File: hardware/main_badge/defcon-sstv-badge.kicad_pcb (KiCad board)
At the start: 4 copper layers, 185.7 x 199 mm, 136 parts, among them J1 Conn_01x02, J10 Micro_SD_Card, J11 Mechanical/Grounds, J12 Mechanical/Grounds, J2 USB4105-GF-A, J3 ILI9341 Display Module, J4 Conn_02x09_Odd_Even, J5 SAO1, J6 SAO2, J7 Conn_01x08_Socket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

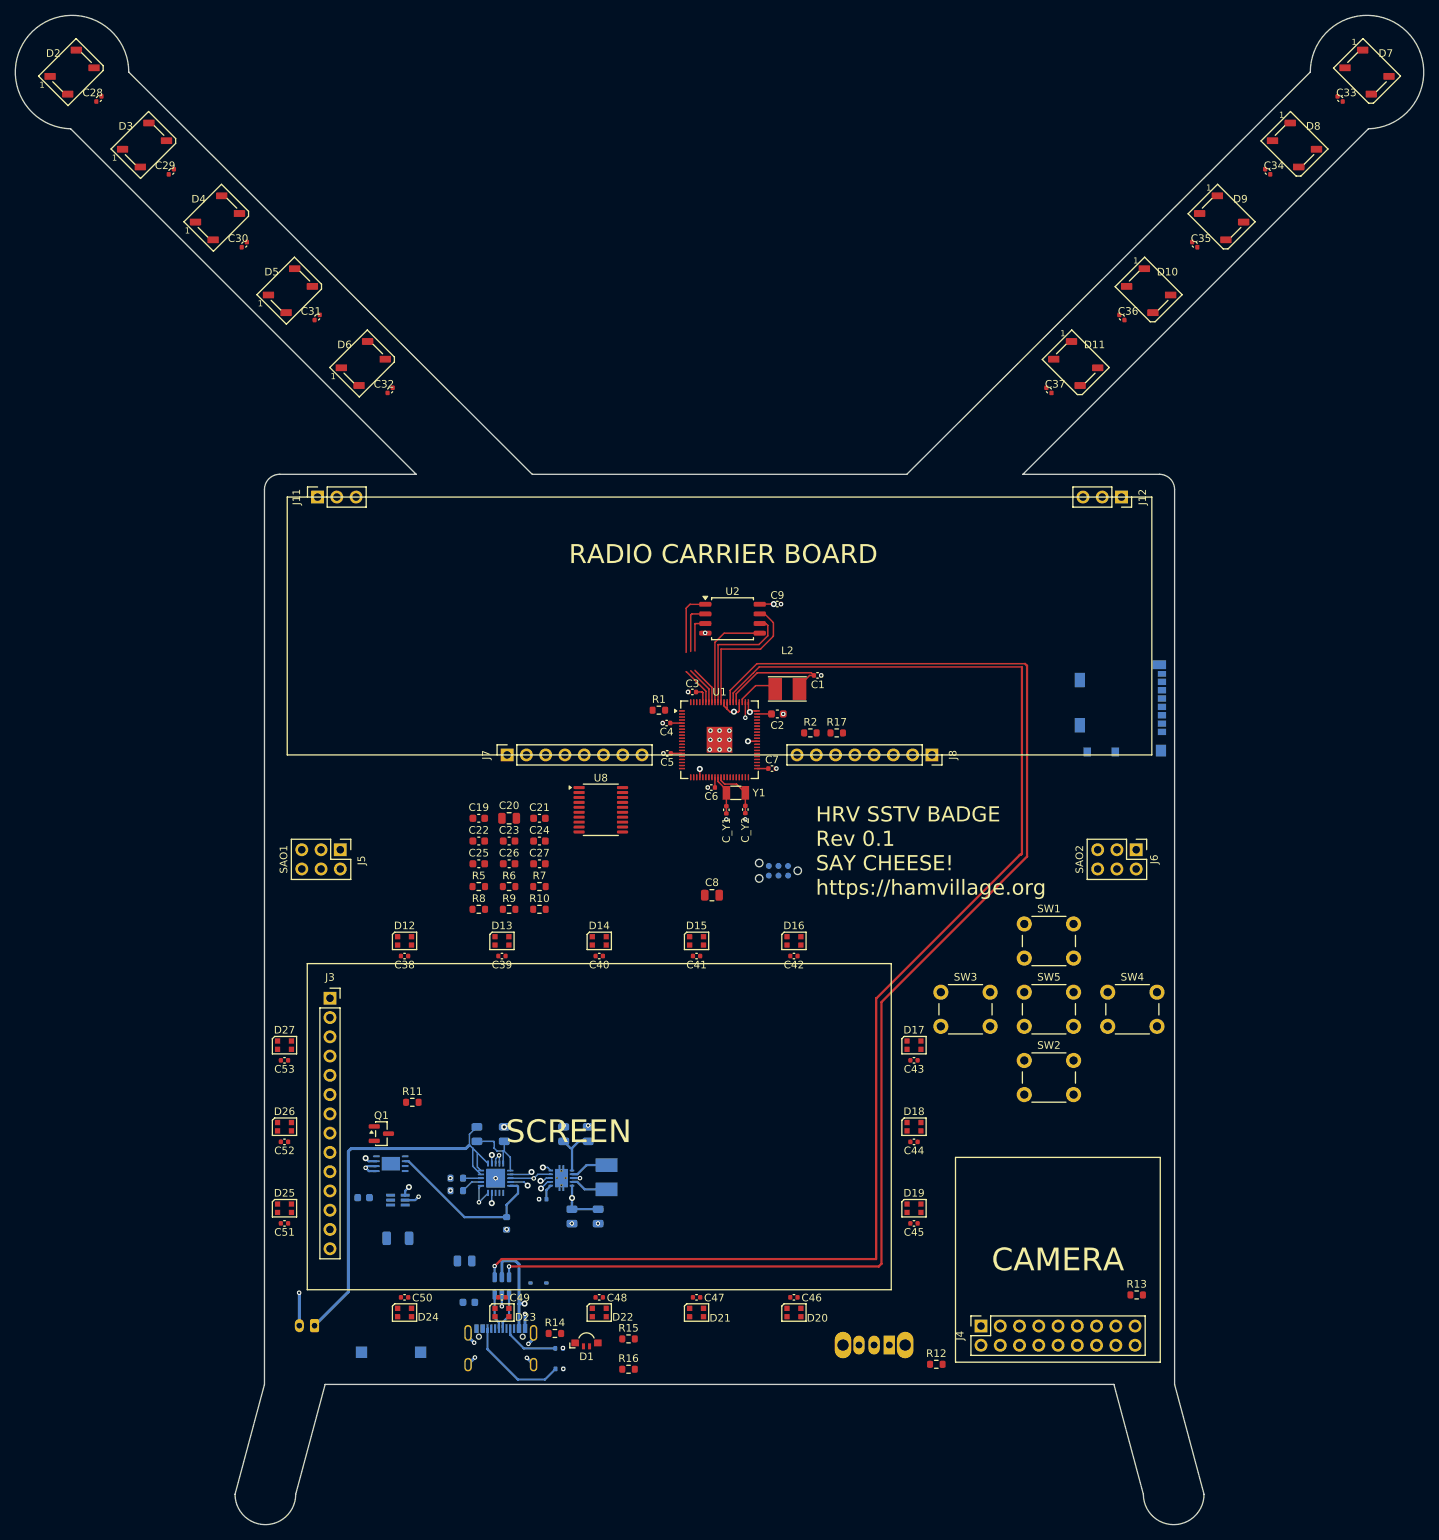
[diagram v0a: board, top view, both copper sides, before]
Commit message: traces all fubar, might delete them all and start over.
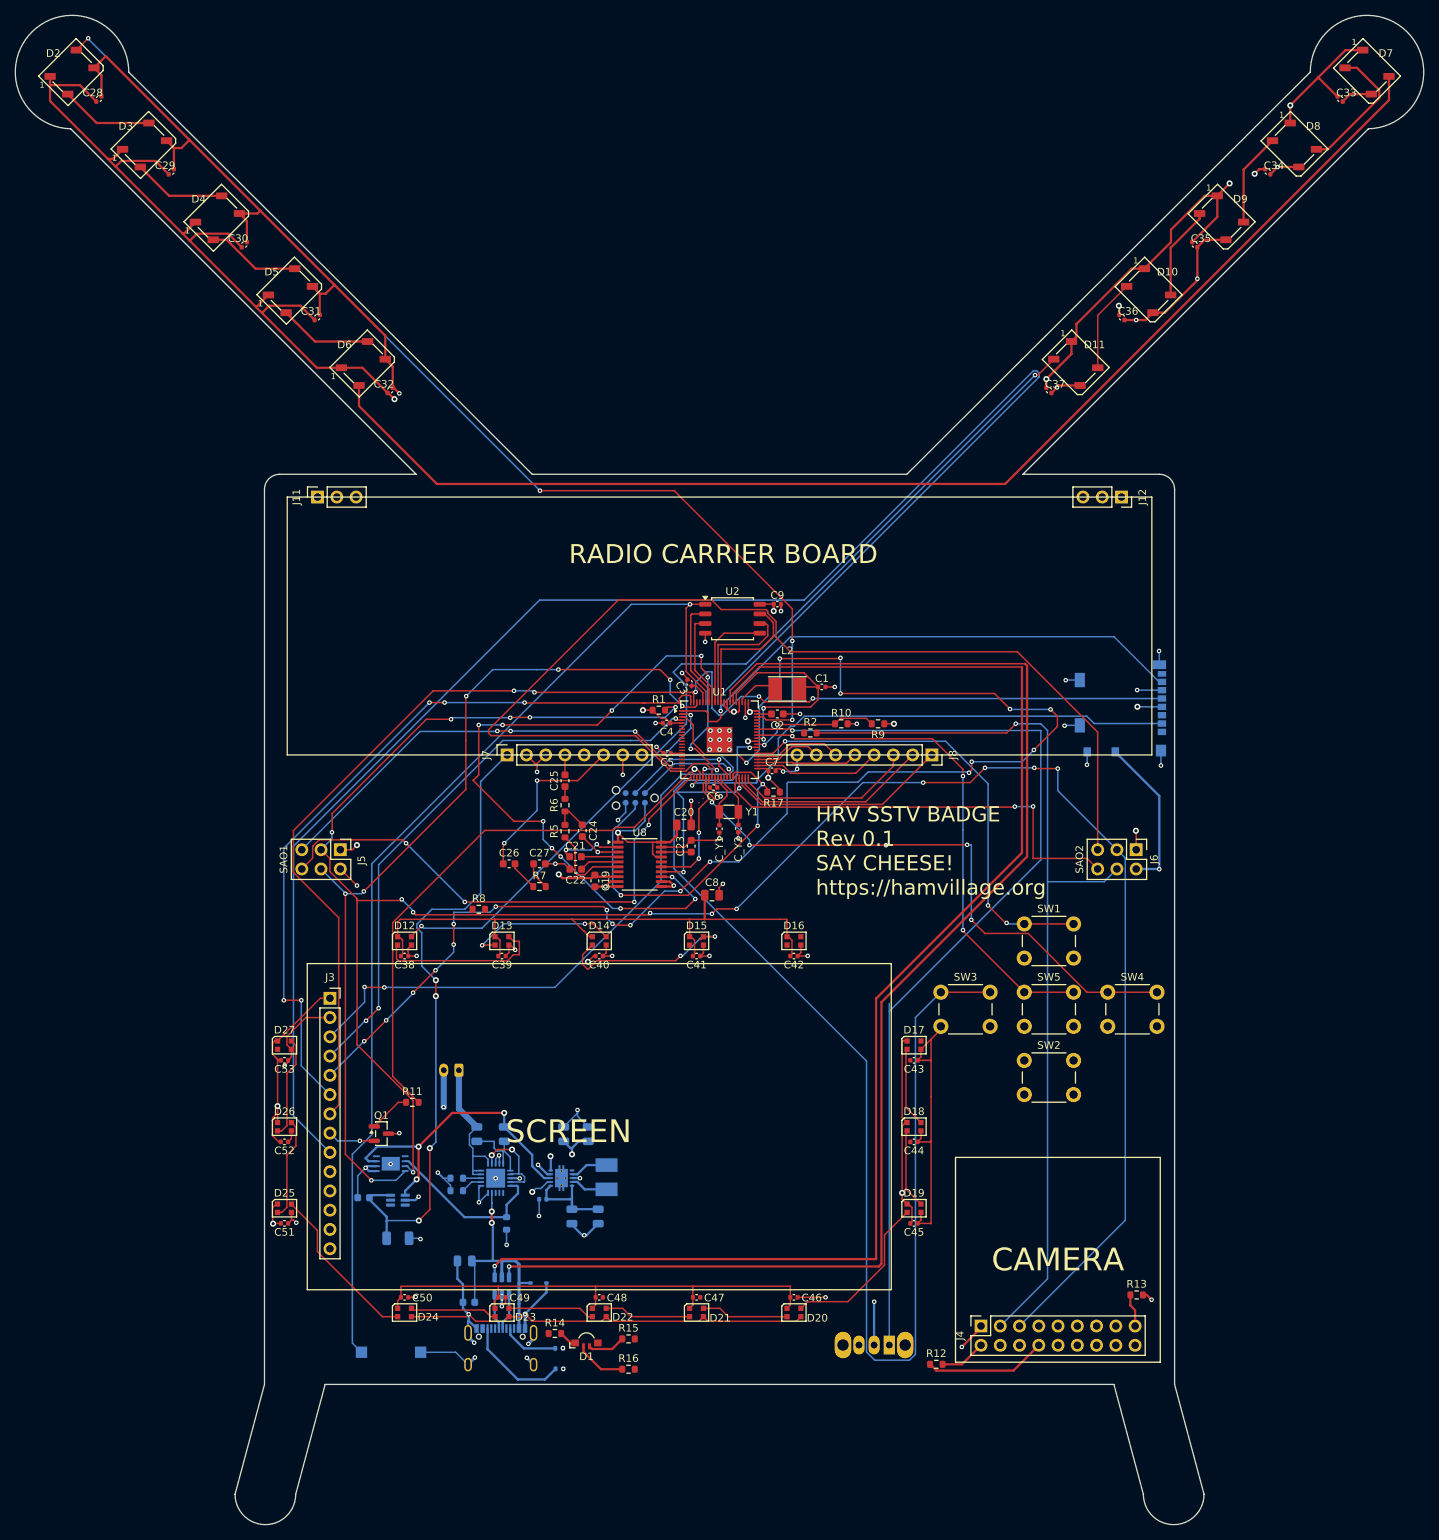
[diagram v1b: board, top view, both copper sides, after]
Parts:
- moved R9 54.4 mm to (80.9, 32.9), turned to 180 degrees
- moved R10 46.7 mm to (76.0, 32.9)
- moved J1 38.7 mm to (25.6, 78.6)
- moved C23 24.0 mm to (56.3, 49.0), turned to 90 degrees
- moved C20 23.1 mm to (55.3, 46.2)
- moved J9 21.2 mm to (48.9, 42.7)
- moved C19 17.4 mm to (43.6, 53.6), turned to -90 degrees
- moved C25 15.8 mm to (39.6, 40.4), turned to 90 degrees
- moved R5 13.5 mm to (39.6, 47.1), turned to 90 degrees
- moved C22 13.3 mm to (41.0, 52.1), turned to 180 degrees
- moved R6 13.0 mm to (39.6, 43.6), turned to 90 degrees
- moved R17 11.4 mm to (67.1, 41.9), turned to 180 degrees
- moved U8 8.83 mm to (49.5, 51.4)
- moved C21 6.94 mm to (41.0, 50.4)
- moved C24 5.82 mm to (41.9, 47.0), turned to -90 degrees
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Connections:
- U1 pad 38: SA818_TX -> SA818_RX
- U1 pad 39: SA818_RX -> SA818_TX
- U1 pad 44: SA818_SQ -> SA818_ID
- U1 pad 45: SA818_ID -> SA818_SQ
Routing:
- net +3V3: track 32.7 -> 462.3 mm, vias 7 -> 26
- net GND: track 46.4 -> 441.4 mm, vias 45 -> 78
- net SPI_MISO: track 0.00 -> 301.2 mm, vias 0 -> 1
- net I2C_SDA: track 0.00 -> 291.4 mm, vias 0 -> 15
- net I2C_SCL: track 0.00 -> 240.4 mm, vias 0 -> 8
- net DISP_DC: track 0.00 -> 195.7 mm, vias 0 -> 21
- net SPI_SCK: track 0.00 -> 172.4 mm, vias 0 -> 5
- net Net-(D6-DOUT): track 0.00 -> 166.9 mm
- net DPAD_LEFT: track 0.00 -> 162.9 mm, vias 0 -> 1
- net LED_DATA: track 0.00 -> 145.8 mm, vias 0 -> 4
- net SAO2_GPIO1: track 0.00 -> 145.2 mm
- net AIRPLANE: track 0.00 -> 127.8 mm, vias 0 -> 1
- net Net-(U1-~{QSPI_SS}): track 13.7 -> 138.3 mm, vias 0 -> 1
- net Net-(D11-DOUT): track 0.00 -> 122.9 mm, vias 0 -> 2
- net I2S_BCK: track 0.00 -> 105.7 mm, vias 0 -> 14
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- added copper zone on In1.Cu, net GND

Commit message: clean PCB, prior to rewiring for clean board design
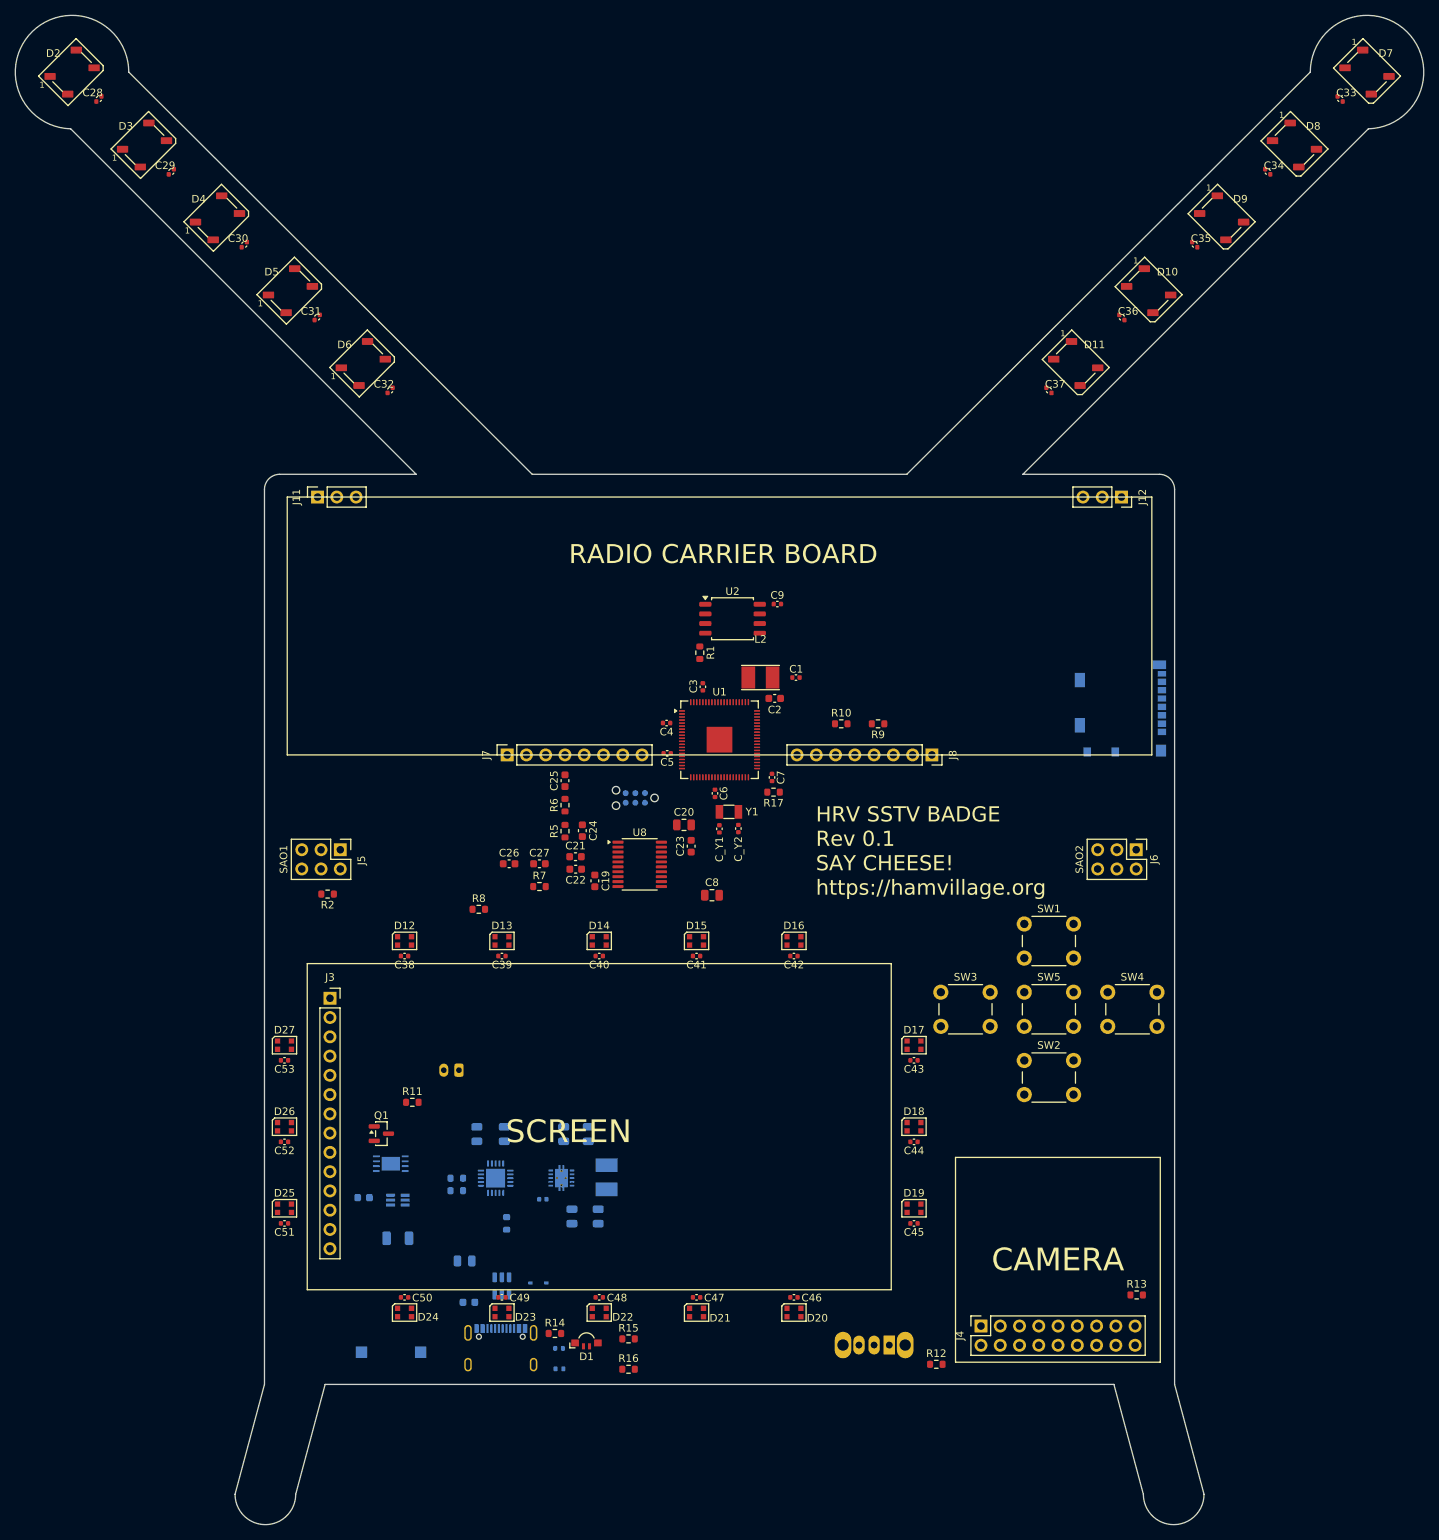
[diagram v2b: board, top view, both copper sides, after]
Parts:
- moved R2 67.1 mm to (8.32, 55.4), turned to 180 degrees
- moved R1 9.30 mm to (57.4, 23.5), turned to -90 degrees
- moved L2 3.84 mm to (65.4, 26.8)
- moved C1 3.61 mm to (70.1, 26.8)
- moved C2 2.08 mm to (67.3, 29.6)
- moved C3 1.83 mm to (57.8, 28.0), turned to 90 degrees
- moved C7 0.87 mm to (66.9, 40.0), turned to -90 degrees
- moved C6 0.79 mm to (59.4, 42.1), turned to -90 degrees
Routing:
- net +3V3: track 462.3 -> 0.00 mm, vias 26 -> 0
- net GND: track 441.4 -> 0.00 mm, vias 78 -> 0
- net SPI_MISO: track 301.2 -> 0.00 mm, vias 1 -> 0
- net I2C_SDA: track 291.4 -> 0.00 mm, vias 15 -> 0
- net I2C_SCL: track 240.4 -> 0.00 mm, vias 8 -> 0
- net DISP_DC: track 195.7 -> 0.00 mm, vias 21 -> 0
- net USB_DP: track 179.7 -> 0.00 mm, vias 1 -> 0
- net USB_DM: track 178.9 -> 0.00 mm, vias 1 -> 0
- net SPI_SCK: track 172.4 -> 0.00 mm, vias 5 -> 0
- net Net-(D6-DOUT): track 166.9 -> 0.00 mm
- net DPAD_LEFT: track 162.9 -> 0.00 mm, vias 1 -> 0
- net LED_DATA: track 145.8 -> 0.00 mm, vias 4 -> 0
- net SAO2_GPIO1: track 145.2 -> 0.00 mm
- net Net-(U1-~{QSPI_SS}): track 138.3 -> 0.00 mm, vias 1 -> 0
- net AIRPLANE: track 127.8 -> 0.00 mm, vias 1 -> 0
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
